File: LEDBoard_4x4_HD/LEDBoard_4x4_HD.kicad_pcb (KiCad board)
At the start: 4 copper layers, 33 x 13.6 mm, 23 parts, among them J1 power, J2 data, U1 TLC5957

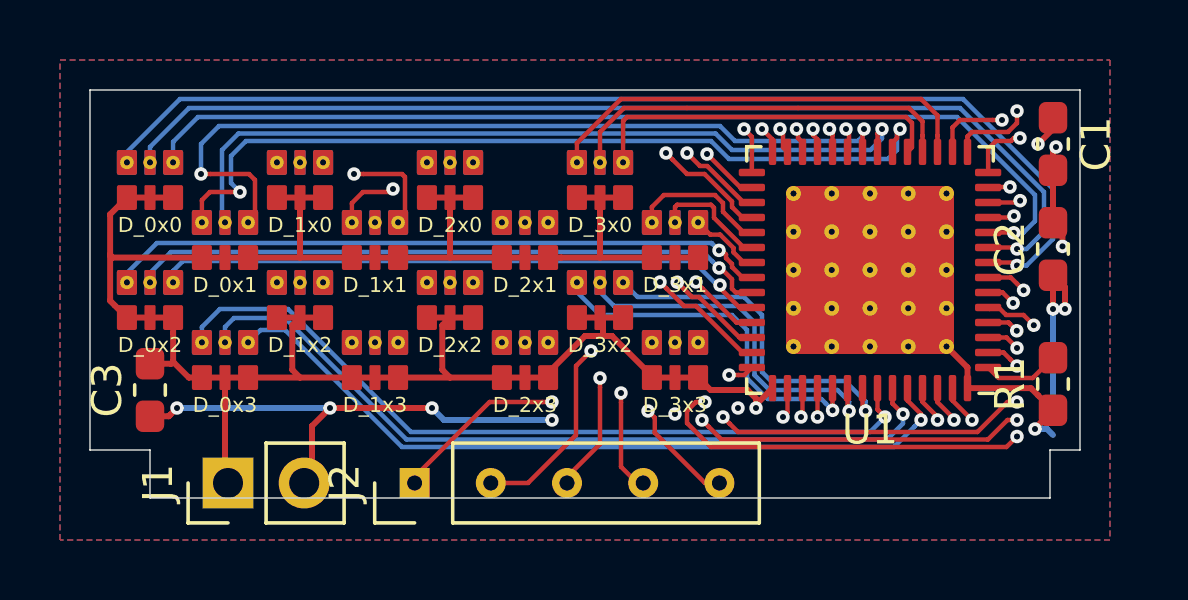
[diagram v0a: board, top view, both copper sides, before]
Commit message: updated pcb fixed some small things added capacitor
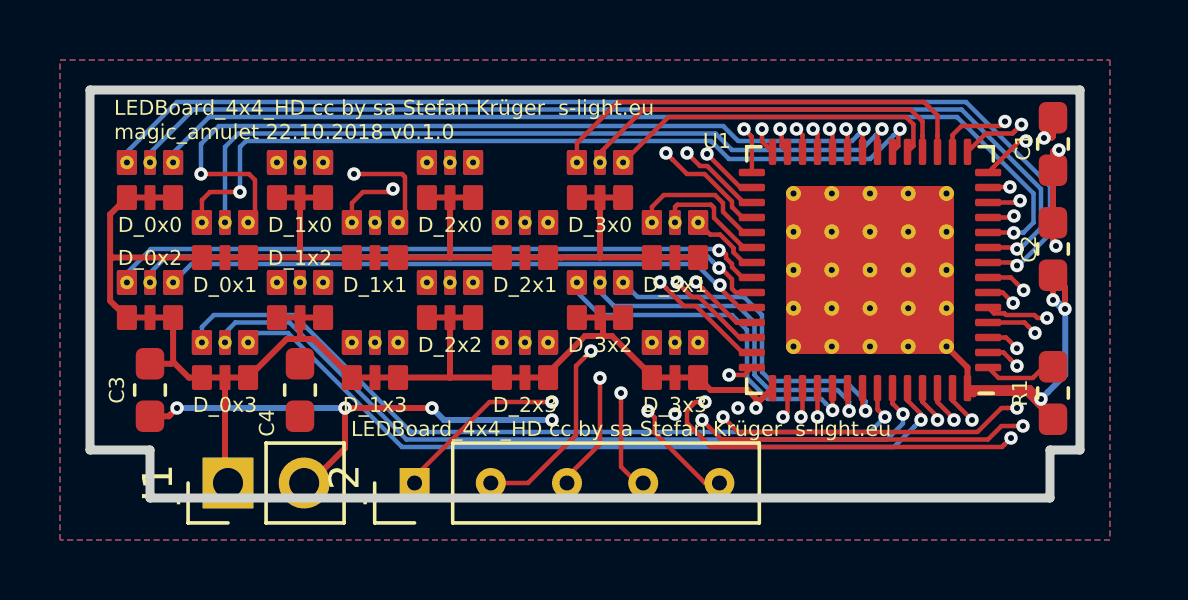
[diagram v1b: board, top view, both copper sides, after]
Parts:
- added C4: 47uF 6.3V, Capacitor_SMD:C_0603_1608Metric_Pad1.05x0.95mm_HandSolder, F.Cu at (107.0, 110.0)
- C1: value 0.1uF -> 47uF 6.3V
- moved R1 0.30 mm to (132.1, 110.1)
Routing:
- net VCC: track 100.6 -> 95.2 mm
- net GND: track 45.1 -> 50.4 mm
- net /led_1x1_r: track 20.3 -> 19.1 mm
- net /led_2x3_b: track 23.2 -> 24.4 mm
- net /led_1x0_g: track 28.7 -> 27.8 mm
- net /led_1x0_b: track 26.3 -> 25.5 mm
- net /led_3x3_r: track 21.5 -> 22.3 mm
- net /led_3x0_b: track 12.2 -> 11.4 mm
- net /led_0x1_r: track 27.8 -> 27.2 mm
- net /led_3x3_g: track 19.6 -> 20.2 mm
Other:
- board text added: "LEDBoard_4x4_HD cc by sa Stefan Krüger s-light.eu"
- board text added: "LEDBoard_4x4_HD cc by sa Stefan Krüger s-light.eu magic_amulet 22.10.2018 v0.1.0"

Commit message: more layout tweeks + separate VCC for controler
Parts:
- added J3: power, PCB_SolderMount:Conn_01x02_SMD_90deg_SolderMount, F.Cu at (127.3, 112.8)
- J1: footprint Connector_PinHeader_2.54mm:PinHeader_1x02_P2.54mm_Vertical -> PCB_SolderMount:Conn_01x02_SMD_90deg_SolderMount
- J2: footprint Connector_PinHeader_2.54mm:PinHeader_1x05_P2.54mm_Vertical -> PCB_SolderMount:Conn_01x05_SMD_90deg_SolderMount
- moved J2 5.69 mm to (116.5, 112.8), turned to 0 degrees
- moved J1 1.14 mm to (105.7, 112.8), turned to 0 degrees
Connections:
- C3 pad 2: VCC -> VCC_LED
- C4 pad 2: VCC -> VCC_LED
- D_0x0 pad 4: VCC -> VCC_LED
- D_0x0 pad 5: VCC -> VCC_LED
- D_0x0 pad 6: VCC -> VCC_LED
- D_0x1 pad 4: VCC -> VCC_LED
- D_0x1 pad 5: VCC -> VCC_LED
- D_0x1 pad 6: VCC -> VCC_LED
- D_0x2 pad 4: VCC -> VCC_LED
- D_0x2 pad 5: VCC -> VCC_LED
- D_0x2 pad 6: VCC -> VCC_LED
- D_0x3 pad 4: VCC -> VCC_LED
- D_0x3 pad 5: VCC -> VCC_LED
- D_0x3 pad 6: VCC -> VCC_LED
- D_1x0 pad 4: VCC -> VCC_LED
- D_1x0 pad 5: VCC -> VCC_LED
- D_1x0 pad 6: VCC -> VCC_LED
- D_1x1 pad 4: VCC -> VCC_LED
- D_1x1 pad 5: VCC -> VCC_LED
- D_1x1 pad 6: VCC -> VCC_LED
- D_1x2 pad 4: VCC -> VCC_LED
- D_1x2 pad 5: VCC -> VCC_LED
- D_1x2 pad 6: VCC -> VCC_LED
- D_1x3 pad 4: VCC -> VCC_LED
- D_1x3 pad 5: VCC -> VCC_LED
- D_1x3 pad 6: VCC -> VCC_LED
- D_2x0 pad 4: VCC -> VCC_LED
- D_2x0 pad 5: VCC -> VCC_LED
- D_2x0 pad 6: VCC -> VCC_LED
- D_2x1 pad 4: VCC -> VCC_LED
- D_2x1 pad 5: VCC -> VCC_LED
- D_2x1 pad 6: VCC -> VCC_LED
- D_2x2 pad 4: VCC -> VCC_LED
- D_2x2 pad 5: VCC -> VCC_LED
- D_2x2 pad 6: VCC -> VCC_LED
- D_2x3 pad 4: VCC -> VCC_LED
- D_2x3 pad 5: VCC -> VCC_LED
- D_2x3 pad 6: VCC -> VCC_LED
- D_3x0 pad 4: VCC -> VCC_LED
- D_3x0 pad 5: VCC -> VCC_LED
- D_3x0 pad 6: VCC -> VCC_LED
- D_3x1 pad 4: VCC -> VCC_LED
- D_3x1 pad 5: VCC -> VCC_LED
- D_3x1 pad 6: VCC -> VCC_LED
- D_3x2 pad 4: VCC -> VCC_LED
- D_3x2 pad 5: VCC -> VCC_LED
- D_3x2 pad 6: VCC -> VCC_LED
- D_3x3 pad 4: VCC -> VCC_LED
- D_3x3 pad 5: VCC -> VCC_LED
- D_3x3 pad 6: VCC -> VCC_LED
- J1 pad 1: VCC -> VCC_LED
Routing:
- net VCC_LED: track 0.00 -> 78.8 mm, vias 0 -> 12
- net VCC: track 95.2 -> 41.3 mm
- net GND: track 50.4 -> 67.8 mm, vias 10 -> 17
- net /led_3x3_b: track 22.3 -> 23.9 mm
- net /SOUT: track 7.53 -> 9.12 mm
- net /led_3x2_b: track 12.0 -> 10.7 mm
- net /led_3x2_g: track 12.3 -> 11.1 mm
- net /led_2x3_b: track 24.4 -> 23.4 mm
- net /led_3x2_r: track 12.2 -> 11.1 mm
- net /SCLK: track 19.5 -> 18.6 mm
- net /led_3x3_r: track 22.3 -> 21.4 mm
- net /led_0x3_b: track 25.8 -> 24.9 mm
- net /led_1x3_b: track 22.7 -> 21.9 mm
- net /GCLK: track 22.0 -> 21.3 mm
- net /led_1x3_r: track 23.2 -> 22.6 mm
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- added copper zone on F.Cu, net GND
- added copper zone on F.Cu, net VCC_LED
- added copper zone on In1.Cu, net VCC_LED
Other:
- outline, holes or cut-outs redrawn
- board text added: "GCLK SCLK LAT SIN SOUT"
- board text added: "GND VCC"
- board text added: "LEDBoard_4x4_HD cc by sa Stefan Krüger s-light.eu magic_amulet 22.10.2018 v1.0.0"
- board text added: "SOUT SIN LAT SCLK GCLK"
- board text added: "VCC GND"
- board text removed: "LEDBoard_4x4_HD cc by sa Stefan Krüger s-light.eu"
- board text removed: "LEDBoard_4x4_HD cc by sa Stefan Krüger s-light.eu magic_amulet 22.10.2018 v0.1.0"

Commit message: some more clean up and exporting
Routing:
- net GND: track 67.8 -> 163.9 mm, vias 17 -> 32
- net VCC_LED: track 78.8 -> 139.3 mm, vias 12 -> 23
- net /led_1x0_r: track 30.8 -> 30.0 mm
- net /led_2x1_b: track 10.6 -> 11.3 mm
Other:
- rule pad_to_mask_clearance: 0.051 -> 0
- rule solder_mask_min_width: 0.25 -> 0.1

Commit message: fixed silk print
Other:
- board text added: "LEDBoard_4x4_HD cc by sa Stefan Krüger s-light.eu"
- board text added: "magic_amulet 22.10.2018 v1.0.0"
